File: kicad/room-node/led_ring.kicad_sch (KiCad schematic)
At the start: 0 parts

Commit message: SQU-27: Draw rev A schematic (6 sheets + root hierarchy)
- Draw mcu, audio_out, microphone, led_ring, sensors and display sheets
  from docs/pcb/schematic.md: doc refs, values, footprints, MPN and LCSC
  fields. The old MCU sheet (2xx refs, wiring errors) is redrawn.
- Root sheet now holds the 6 sheets as a normal hierarchy; the project
  no longer lists every file as a KiCad 10 top-level sheet, so project
  ERC and netlist cover all sheets.
- Project library: replace the wrong 4-pin AHT20 with a 6-pin symbol and
  6-pad footprint from LCSC C2757850 (pin 1 top-left, datasheet v1.1 s3);
  remove the wrong SPH0645 part (stock part is used); fix the library
  header so KiCad can load it (kicad_symbol_lib, version 20251024).
- tools/check_pinout.py: checks the netlist against pinout.md and the
  other end of each net against schematic.md.
- reports/schematic: ERC report (0 errors, 1 warning), netlist check
  (PASS), PDF of all 7 sheets.
- schematic.md: update status, refs and library notes.

Co-Authored-By: Claude Opus 5.5 <noreply@anthropic.com>
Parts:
- added C30: 1000µF 16V, Capacitor_THT:CP_Radial_D10.0mm_P5.00mm, symbol Device:C_Polarized
- added J4: LED strip, Connector_JST:JST_XH_B3B-XH-A_1x03_P2.50mm_Vertical, symbol Connector_Generic:Conn_01x03
- added R30: 470Ω, Resistor_SMD:R_0603_1608Metric, symbol Device:R
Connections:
- new net: J4.2 (Pin_2), R30.2
- new net +5V: C30.1, J4.1 (Pin_1)
- new net GND: C30.2, J4.3 (Pin_3)
- new net LED_DIN: R30.1
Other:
- note added: "J4: 1 = +5V, 2 = DIN, 3 = GND. JST-XH 3 A; full white is ~1.6 A. R30 near U1. C30 across J4 pins 1 and 3, at J4. Strip: 27 x WS2812B, off-board. No level shifter (works on the breadboard); if the strip flickers on rev A, rev B adds a 74AHCT125."
- note added: "WS2812B LED strip connector"
- company: (none) -> Squarewave Labs
- title: (none) -> Room node rev A - LED ring

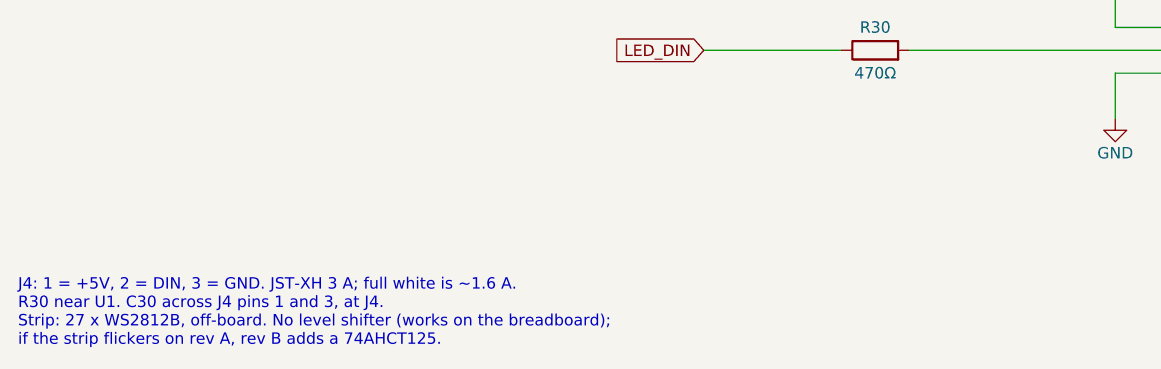
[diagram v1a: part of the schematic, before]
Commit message: SQU-42: J4 LED connector to side entry (S3B-XH-A), cable out of the bottom edge
- J4 footprint JST_XH_B3B-XH-A vertical -> JST_XH_S3B-XH-A_1x03_P2.50mm_Horizontal
  (JST S3B-XH-A(LF)(SN), LCSC C157928, 3 A), mouth facing the bottom edge.
  Pins at (124.0/126.5/129.0, 128.45); housing front 0.30 mm inside the edge, no
  body overhang; silk 0.18 mm off the edge. Pin order unchanged (1 +5V, 2 DIN, 3 GND).
- J4 courtyard -> U6 courtyard 18.81 mm, -> island slot 15.60 mm (unchanged).
  C30 stays at J4 (courtyards 0.21 mm, C30+ -> pin 1 7.08 mm).
- TP1-TP7 + D1 into a 2 x 4 block right of J4 (the housing covers the old row);
  TP6 (+5V) still drops straight onto the spine.
- Full pipeline re-run (Freerouting 2.4.1 / Temurin 25); Gerbers, renders, DRC/ERC
  reports and schematic PDF regenerated. BOM, schematic.md, layout.md updated.
  DRC 0 errors / 0 unconnected / 0 parity (12 silk warnings, same set as main),
  ERC 0 errors (1 known warning), check_pinout PASS.

Co-Authored-By: Claude Opus 5.5 <noreply@anthropic.com>
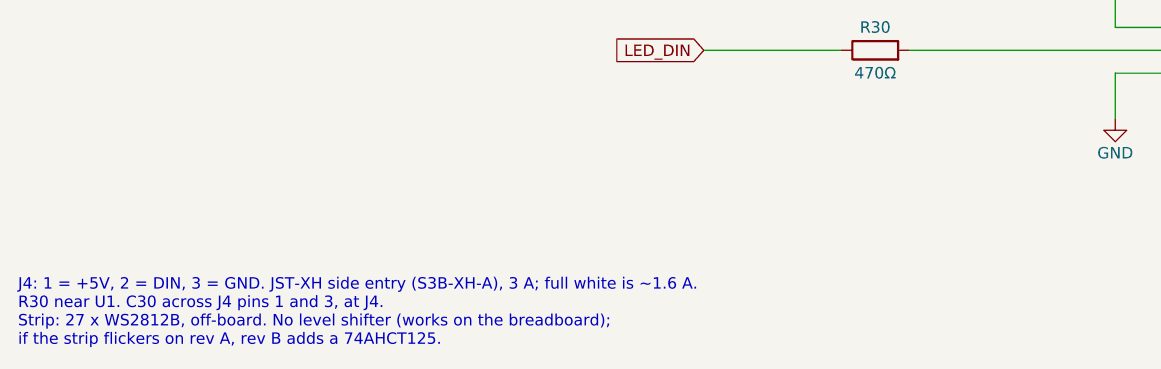
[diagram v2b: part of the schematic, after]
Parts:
- J4: footprint Connector_JST:JST_XH_B3B-XH-A_1x03_P2.50mm_Vertical -> Connector_JST:JST_XH_S3B-XH-A_1x03_P2.50mm_Horizontal; LCSC TBD -> C157928; MPN JST B3B-XH-A -> JST S3B-XH-A(LF)(SN)
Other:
- note added: "J4: 1 = +5V, 2 = DIN, 3 = GND. JST-XH side entry (S3B-XH-A), 3 A; full white is ~1.6 A. R30 near U1. C30 across J4 pins 1 and 3, at J4. Strip: 27 x WS2812B, off-board. No level shifter (works on the breadboard); if the strip flickers on rev A, rev B adds a 74AHCT125."
- note removed: "J4: 1 = +5V, 2 = DIN, 3 = GND. JST-XH 3 A; full white is ~1.6 A. R30 near U1. C30 across J4 pins 1 and 3, at J4. Strip: 27 x WS2812B, off-board. No level shifter (works on the breadboard); if the strip flickers on rev A, rev B adds a 74AHCT125."
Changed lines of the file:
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@@
 			)
 		)
-		(property "Footprint" "Connector_JST:JST_XH_B3B-XH-A_1x03_P2.50mm_Vertical"
+		(property "Footprint" "Connector_JST:JST_XH_S3B-XH-A_1x03_P2.50mm_Horizontal"
 			(at 162.56 101.6 0)
 			(hide yes)
@@
 			)
 		)
-		(property "MPN" "JST B3B-XH-A"
+		(property "MPN" "JST S3B-XH-A(LF)(SN)"
 			(at 162.56 101.6 0)
 			(hide yes)
@@
 			)
 		)
-		(property "LCSC" "TBD"
+		(property "LCSC" "C157928"
 			(at 162.56 101.6 0)
 			(hide yes)
@@
 		)
 	)
-	(text "J4: 1 = +5V, 2 = DIN, 3 = GND. JST-XH 3 A; full white is ~1.6 A.\nR30 near U1. C30 across J4 pins 1 and 3, at J4.\nStrip: 27 x WS2812B, off-board. No level shifter (works on the breadboard);\nif the strip flickers on rev A, rev B adds a 74AHCT125."
+	(text "J4: 1 = +5V, 2 = DIN, 3 = GND. JST-XH side entry (S3B-XH-A), 3 A; full white is ~1.6 A.\nR30 near U1. C30 across J4 pins 1 and 3, at J4.\nStrip: 27 x WS2812B, off-board. No level shifter (works on the breadboard);\nif the strip flickers on rev A, rev B adds a 74AHCT125."
 		(exclude_from_sim no)
 		(at 25.4 127 0)
